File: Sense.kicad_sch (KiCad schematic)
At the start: 10 parts, among them J1 Callistated 1, J2 Callistated 2, U1 SPL07, U2 MMC5603NJ, U3 LSM6DSO32

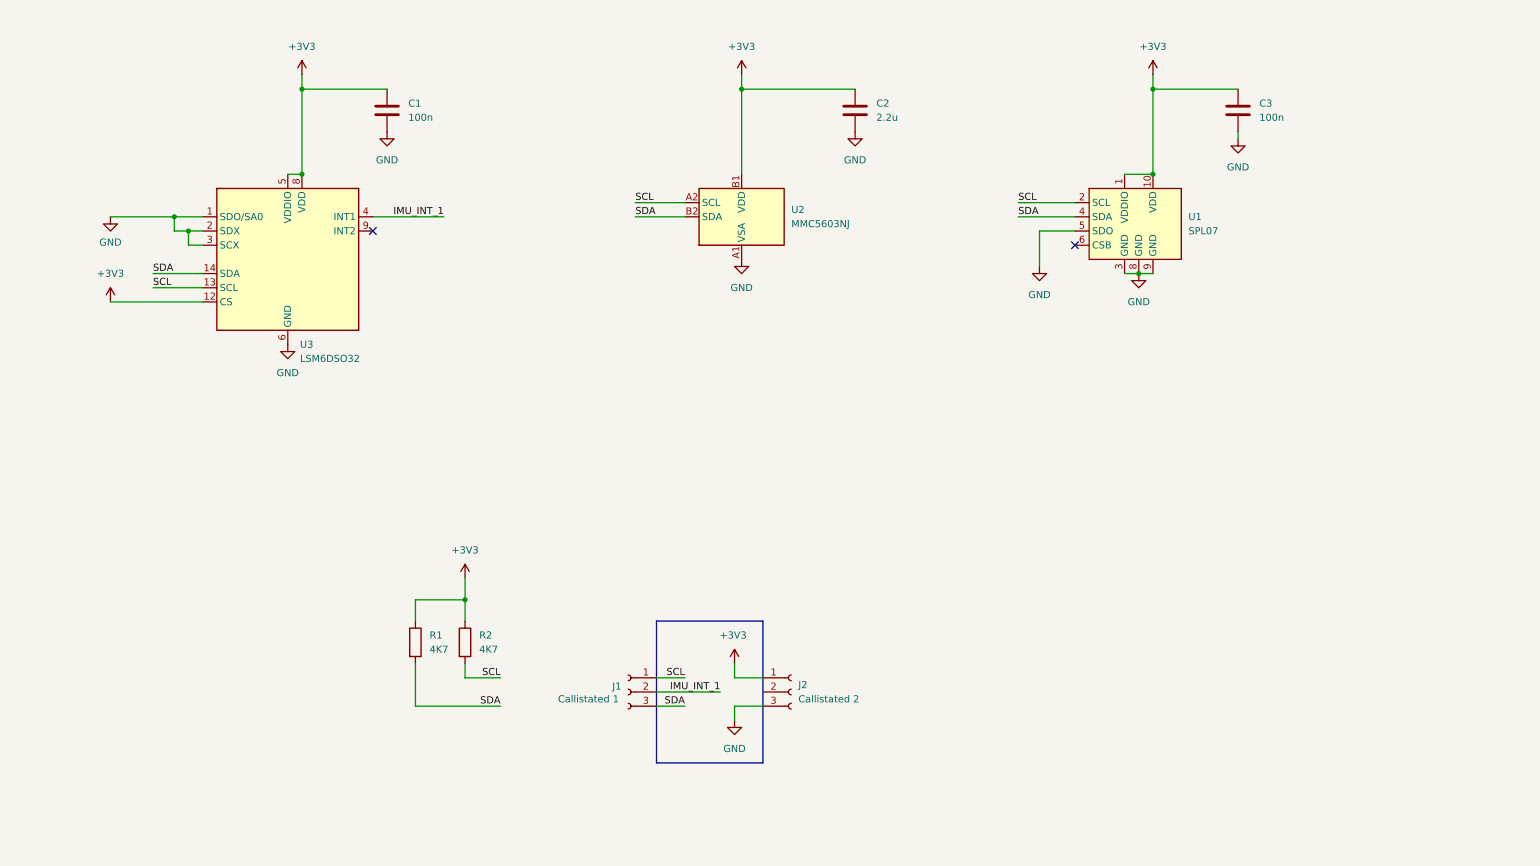
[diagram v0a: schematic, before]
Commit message: Abandoned castellated pads, updated with LCSC parts
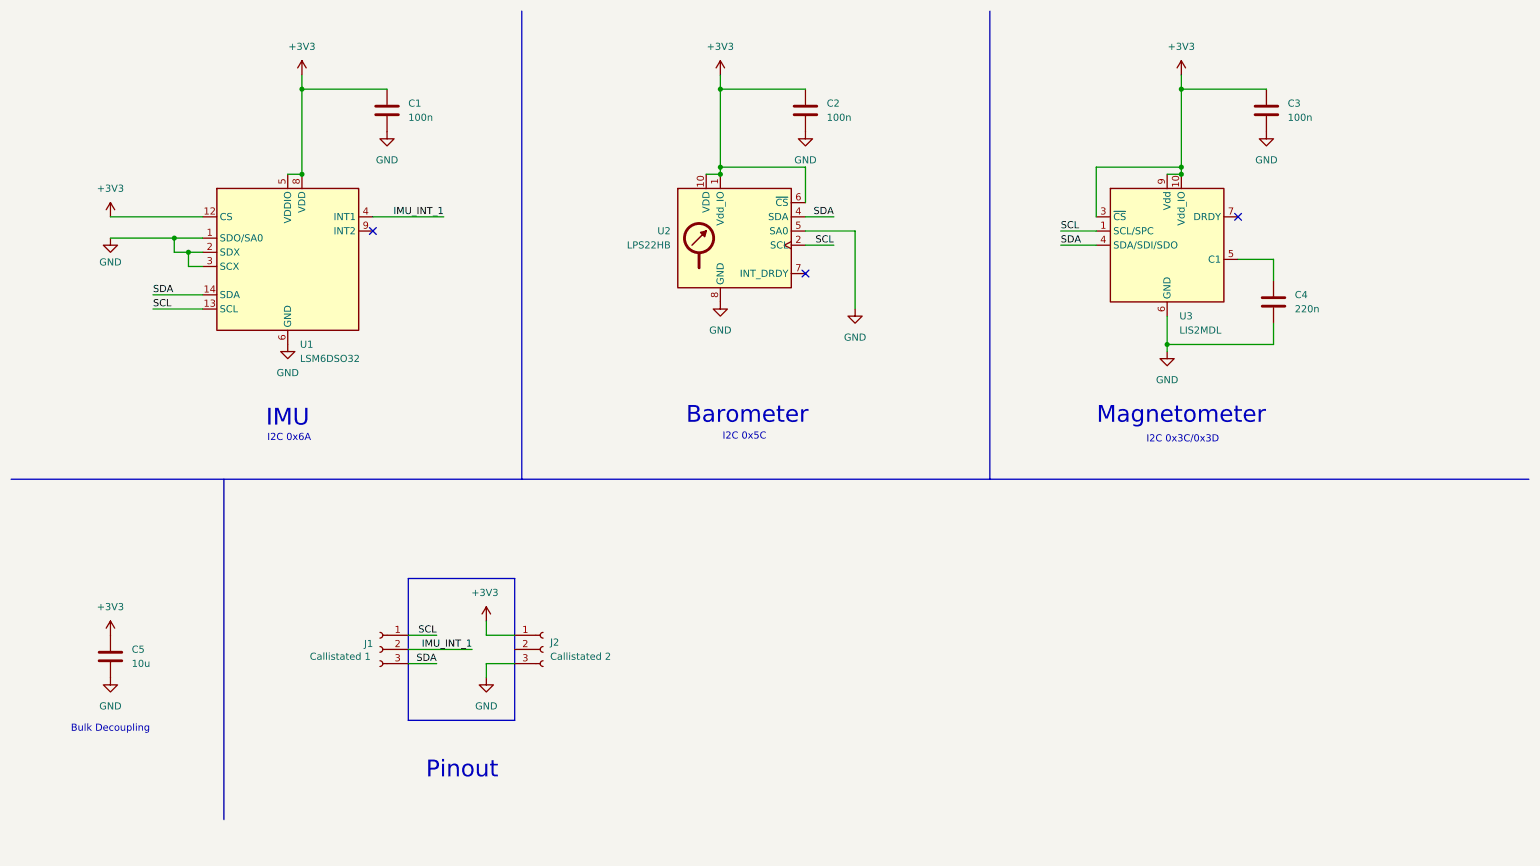
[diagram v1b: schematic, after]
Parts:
- removed R1, R2: 4K7, Resistor_SMD:R_0402_1005Metric, symbol Device:R
- removed U1: SPL07, Package_LGA:ST_HLGA-10_2x2mm_P0.5mm_LayoutBorder3x2y, symbol Sensor_Pressure:SPL07
- removed U2: MMC5603NJ, Package_BGA:WLP-4_0.86x0.86mm_P0.4mm, symbol Sensor_Magnetic:MMC5633NJL
- added C4: 220n, Capacitor_SMD:C_0402_1005Metric, symbol Device:C
- added C5: 10u, Capacitor_SMD:C_0402_1005Metric, symbol Device:C
- added U2: LPS22HB, Package_LGA:ST_HLGA-10_2x2mm_P0.5mm_LayoutBorder3x2y, symbol Sensor_Pressure:LPS22HB
- added U3: LIS2MDL, Package_LGA:LGA-12_2x2mm_P0.5mm, symbol Sensor_Magnetic:LIS2MDL
- C2: value 2.2u -> 100n
- U1: renamed from U3; MPN (none) -> C1864162
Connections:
- net +3V3: now also C5.1, U2.1 (Vdd_IO), U2.10 (VDD), U2.6 (~{CS}), U3.10 (Vdd_IO), U3.3 (~{CS}), U3.9 (Vdd)
- net GND: now also C4.2, C5.2, U2.3 (GND), U2.5 (SA0), U2.8 (GND), U2.9 (GND), U3.6 (GND), U3.8 (GND)
- net SCL: now also U2.2 (SCL), U3.1 (SCL/SPC)
- net SDA: now also U2.4 (SDA), U3.4 (SDA/SDI/SDO)
- new net: C4.1, U3.5 (C1)
- no-connect marks 2 -> 3
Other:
- note added: "Barometer"
- note added: "Bulk Decoupling"
- note added: "I2C 0x3C/0x3D"
- note added: "I2C 0x5C"
- note added: "I2C 0x6A"
- note added: "IMU"
- note added: "Magnetometer"
- note added: "Pinout"
- moved on the sheet: J1, J2

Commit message: Version C.0
Added high g accelerometer option
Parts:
- added C6: 100n, Capacitor_SMD:C_0402_1005Metric, symbol Device:C
- added U4: H3LIS100DLTR, Package_LGA:LGA-16_3x3mm_P0.5mm_LayoutBorder3x5y, symbol Sensor_Motion:H3LIS100DLTR
- U1: value LSM6DSO32 -> LSM6DS3TR-C; MPN C1864162 -> C967633
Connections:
- net +3V3: now also C6.1, U4.1 (VDD_IO), U4.14 (VDD), U4.15 (RES_VDD), U4.8 (CS)
- net GND: now also C6.2, U4.10 (RES_GND), U4.12 (GND), U4.13 (GND), U4.16 (GND), U4.5 (GND), U4.7 (SA0)
- net SCL: now also U4.4 (SCL)
- net SDA: now also U4.6 (SDA)
- no-connect marks 3 -> 6
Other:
- note added: "High G Accelerometer"
- note added: "I2C 0x18"
- moved on the sheet: J1, J2

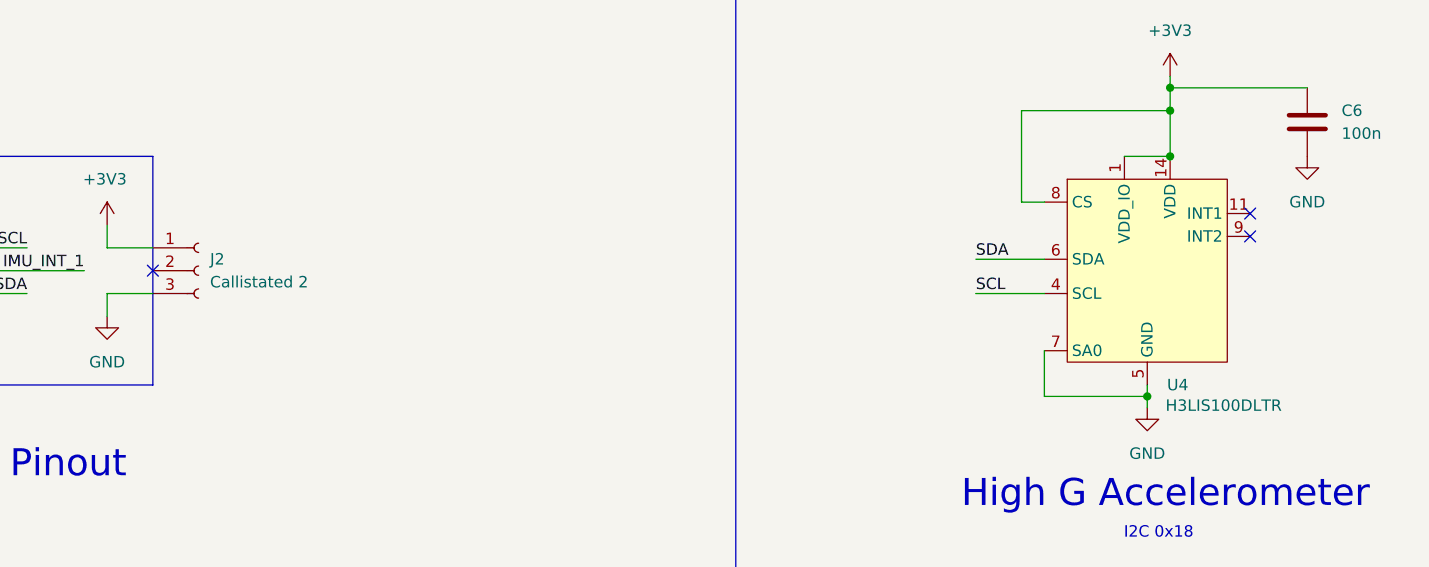
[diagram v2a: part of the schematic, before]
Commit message: Aligned to grid and fixed pin numbering
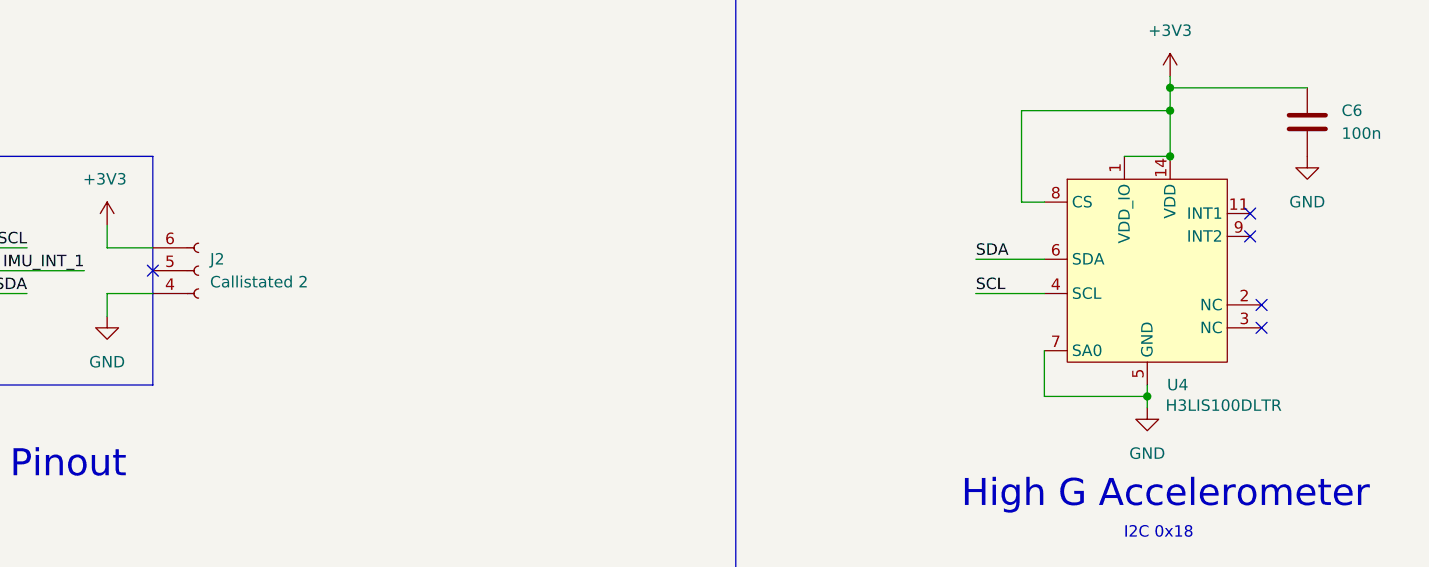
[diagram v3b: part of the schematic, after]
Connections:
- net +3V3: now also J2.6 (Pin_1); no longer J2.1 (Pin_1)
- net GND: now also J2.4 (Pin_3); no longer J2.3 (Pin_3)
- no-connect marks 6 -> 8
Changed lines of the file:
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@@
+	)
+	(no_connect
+		(at 246.38 133.35)
 	)
 	(no_connect
@@
 	(no_connect
 		(at 245.11 125.73)
+	)
+	(no_connect
+		(at 246.38 135.89)
 	)
 	(no_connect
@@
 	)
 	(symbol
+		(lib_name "Conn_01x03_Socket_1")
 		(lib_id "Connector:Conn_01x03_Socket")
 		(at 128.27 129.54 0)
@@
 			)
 		)
-		(pin "2"
-		)
-		(pin "1"
-		)
-		(pin "3"
+		(pin "4"
+		)
+		(pin "6"
+		)
+		(pin "5"
 		)
 		(instances
@@
 		(pin "11"
 		)
+		(pin "2"
+		)
+		(pin "3"
+		)
 		(instances

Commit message: Updated after review
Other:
- note added: "I2C 0x3C/0x3D (R/W)"
- note removed: "I2C 0x3C/0x3D"
- company: B. Redpath -> UC Aerospace
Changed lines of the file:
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@@
 	(title_block
 		(title "MicroSense")
-		(date "2024-04-10")
+		(date "2024-04-17")
 		(rev "C")
-		(company "B. Redpath")
+		(company "UC Aerospace")
+		(comment 1 "Reviewed: K. Adlington")
+		(comment 2 "Drawn: B. Redpath")
 	)
 	(junction
@@
 		)
 	)
-	(text "I2C 0x3C/0x3D"
+	(text "I2C 0x3C/0x3D (R/W)"
 		(exclude_from_sim no)
 		(at 222.504 89.408 0)

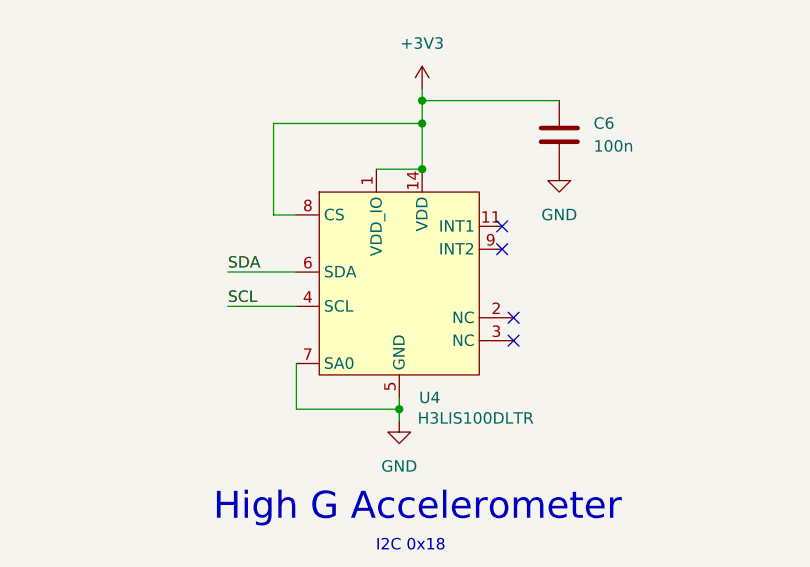
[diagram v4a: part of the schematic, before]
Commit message: Fixed the couple of things that I broke, updated STEP
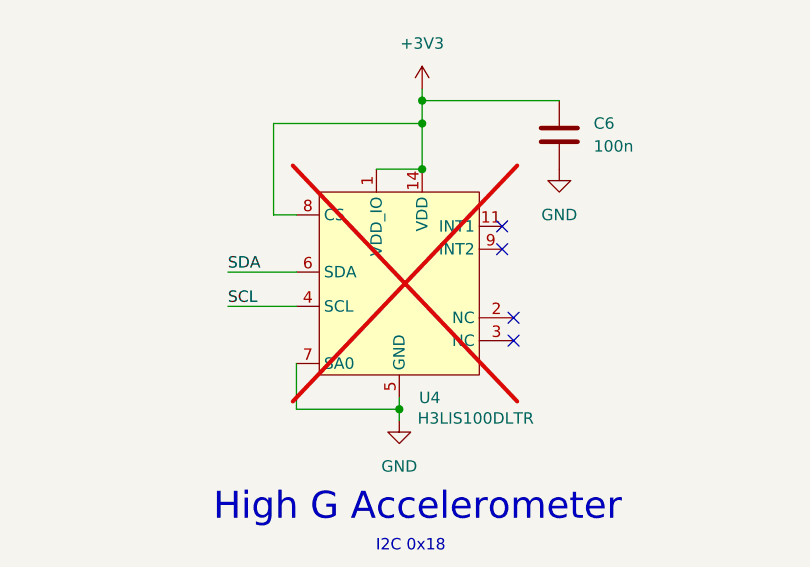
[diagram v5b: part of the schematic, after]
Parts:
- U4: now not fitted
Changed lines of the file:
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@@
 		(in_bom yes)
 		(on_board yes)
-		(dnp no)
+		(dnp yes)
 		(property "Reference" "U4"
 			(at 235.8741 142.24 0)
